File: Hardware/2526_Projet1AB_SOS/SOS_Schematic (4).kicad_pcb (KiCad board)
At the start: 2 copper layers, 64 x 64 mm, 42 parts, among them J1 USB_B_Mini, J2 Conn_02x10_Odd_Even, J3 Conn_01x02, SW1 SW_SPDT, U1 BU33SD5WG-TR, U2 STM32L476RGTx, U3 HTRC11001T, Y1 13,56MHz, Y2 8MHz

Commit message: Add files via upload
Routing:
- net +3.3V: track 236.7 -> 228.6 mm
- net GND: vias 13 -> 134
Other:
- board text added: "B"
- board text added: "Projet SOS"
- board text added: "T"

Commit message: Update KiCAD Schematic: SWD
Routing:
- added copper zone on In2.Cu, net GND
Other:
- copper layers 2 -> 4
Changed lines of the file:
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@@
 	(layers
 		(0 "F.Cu" signal)
+		(4 "In1.Cu" power "In1.Cu - VCC")
+		(6 "In2.Cu" power "In2.Cu -GND")
 		(2 "B.Cu" signal)
 		(9 "F.Adhes" user "F.Adhesive")
@@
 	)
 	(setup
+		(stackup
+			(layer "F.SilkS"
+				(type "Top Silk Screen")
+			)
+			(layer "F.Paste"
+				(type "Top Solder Paste")
+			)
+			(layer "F.Mask"
+				(type "Top Solder Mask")
+				(thickness 0.01)
+			)
+			(layer "F.Cu"
+				(type "copper")
+				(thickness 0.035)
+			)
+			(layer "dielectric 1"
+				(type "prepreg")
+				(thickness 0.1)
+				(material "FR4")
+				(epsilon_r 4.5)
+				(loss_tangent 0.02)
+			)
+			(layer "In1.Cu"
+				(type "copper")
+				(thickness 0.035)
+			)
+			(layer "dielectric 2"
+				(type "core")
+				(thickness 1.24)
+				(material "FR4")
+				(epsilon_r 4.5)
+				(loss_tangent 0.02)
+			)
+			(layer "In2.Cu"
+				(type "copper")
+				(thickness 0.035)
+			)
+			(layer "dielectric 3"
+				(type "prepreg")
+				(thickness 0.1)
+				(material "FR4")
+				(epsilon_r 4.5)
+				(loss_tangent 0.02)
+			)
+			(layer "B.Cu"
+				(type "copper")
+				(thickness 0.035)
+			)
+			(layer "B.Mask"
+				(type "Bottom Solder Mask")
+				(thickness 0.01)
+			)
+			(layer "B.Paste"
+				(type "Bottom Solder Paste")
+			)
+			(layer "B.SilkS"
+				(type "Bottom Silk Screen")
+			)
+			(copper_finish "None")
+			(dielectric_constraints no)
+		)
 		(pad_to_mask_clearance 0)
 		(allow_soldermask_bridges_in_footprints no)
@@
 			)
 		)
+	)
+	(zone
+		(net 1)
+		(net_name "GND")
+		(layer "In2.Cu")
+		(hatch edge 0.5)
+		(priority 1)
+		(connect_pads
+			(clearance 0.5)
+		)
+		(min_thickness 0.25)
+		(filled_areas_thickness no)
+		(fill yes
+			(thermal_gap 0.5)
+			(thermal_bridge_width 0.5)
+		)
+		(polygon
+			(pts
+				(xy 108 67) (xy 172 67) (xy 172 131) (xy 108 131)
+			)
+		)

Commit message: work on schematic and updating board
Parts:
- added R8: 5k1, Resistor_SMD:R_0805_2012Metric_Pad1.20x1.40mm_HandSolder, F.Cu at (157.0, 110.0)
- added R9: 5k1, Resistor_SMD:R_0805_2012Metric_Pad1.20x1.40mm_HandSolder, F.Cu at (157.0, 113.0)
- added U4: USBLC6-2SC6, Package_TO_SOT_SMD:SOT-23-6, F.Cu at (151.0, 111.0)
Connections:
- U2 pad 44: USBDM -> D-
- U2 pad 45: USBDP -> D+
- U2 pad 49: SWDCK -> SWCLK
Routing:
- net USBDM: track 52.4 -> 2.16 mm, vias 2 -> 1
- net D-: track 0.00 -> 49.7 mm, vias 0 -> 1
- net D+: track 0.00 -> 4.84 mm
- net GND: track 191.2 -> 186.6 mm, vias 134 -> 150
- net USBDP: track 44.3 -> 41.3 mm
- net SWDIO: track 30.1 -> 31.4 mm
- net Net-(J2-Pin_17): track 48.4 -> 47.8 mm

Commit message: schematic v2
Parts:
- removed C18, C20: 1u, Capacitor_SMD:C_0603_1608Metric_Pad1.08x0.95mm_HandSolder
- removed C19: 20p, Capacitor_SMD:C_0603_1608Metric_Pad1.08x0.95mm_HandSolder
- removed C8: 22p, Capacitor_SMD:C_0603_1608Metric_Pad1.08x0.95mm_HandSolder
- removed J1: USB_B_Mini, Connector_USB:USB_Mini-B_Tensility_54-00023_Vertical
- removed J3: Conn_01x02, Connector_JST:JST_XH_B2B-XH-A_1x02_P2.50mm_Vertical
- removed L1: 1/2 uH, Inductor_SMD:L_0805_2012Metric_Pad1.05x1.20mm_HandSolder
- removed L2: L_Small, Inductor_SMD:L_0805_2012Metric_Pad1.05x1.20mm_HandSolder
- removed U4: USBLC6-2SC6, Package_TO_SOT_SMD:SOT-23-6
- removed Y2: 8MHz, Crystal:Crystal_DS10_D1.0mm_L4.3mm_Vertical
- added D1: RED, LED_SMD:LED_0603_1608Metric, F.Cu at (91.6, 61.6)
- added D2: RED, LED_SMD:LED_0603_1608Metric, F.Cu at (91.6, 64.2)
- added D3: RED, LED_SMD:LED_0603_1608Metric, F.Cu at (96.2, 83.4)
- added D4: GREEN, LED_SMD:LED_0603_1608Metric, F.Cu at (96.2, 86.0)
- added D5: BLUE, LED_SMD:LED_0603_1608Metric, F.Cu at (96.0, 89.7)
- added R10: 10k, Resistor_SMD:R_0603_1608Metric, F.Cu at (67.0, 32.5)
- added R11: 1k6, Resistor_SMD:R_0603_1608Metric, F.Cu at (91.2, 82.5)
- added R12: 1k1, Resistor_SMD:R_0603_1608Metric, F.Cu at (91.2, 85.0)
- added R13: 10k, Resistor_SMD:R_0603_1608Metric, F.Cu at (67.0, 40.0)
- added R14: 670R, Resistor_SMD:R_0603_1608Metric, F.Cu at (91.2, 90.0)
- added R15: 10k, Resistor_SMD:R_0603_1608Metric, F.Cu at (67.0, 45.0)
- added RFID1: RC522, Connector_PinSocket_2.54mm:PinSocket_1x08_P2.54mm_Vertical, F.Cu at (66.1, 100.0)
- added SW2: SW_Push, Button_Switch_SMD:SW_SPST_B3S-1000, F.Cu at (61.4, 51.0)
- added SW3: SW_Push, Button_Switch_SMD:SW_SPST_B3S-1000, F.Cu at (69.8, 51.0)
- added SW4: SW_Push, Button_Switch_SMD:SW_SPST_B3S-1000, F.Cu at (78.2, 51.0)
- added SW5: SW_Push, Button_Switch_SMD:SW_SPST_B3S-1000, F.Cu at (86.7, 51.0)
- added TP4: TP_NSS, TestPoint:TestPoint_Pad_D1.0mm, F.Cu at (67.5, 93.3)
- added TP5: TP_SCK, TestPoint:TestPoint_Pad_D1.0mm, F.Cu at (69.9, 93.4)
- added TP6: TP_MOSI, TestPoint:TestPoint_Pad_D1.0mm, F.Cu at (72.0, 93.5)
- added TP7: TP_MISO, TestPoint:TestPoint_Pad_D1.0mm, F.Cu at (74.3, 93.6)
- added TP8: TP_IRQ, TestPoint:TestPoint_Pad_D1.0mm, F.Cu at (76.8, 93.5)
- added TP9: TP_RST, TestPoint:TestPoint_Pad_D1.0mm, F.Cu at (80.8, 94.7)
- added TP_3V3: TP_3V3, TestPoint:TestPoint_Pad_D1.0mm, F.Cu at (89.1, 70.8)
- added TP_5V1: TP_5V, TestPoint:TestPoint_Pad_D1.0mm, F.Cu at (89.1, 67.7)
- added TP_NRST1: TP_NRST, TestPoint:TestPoint_Pad_D1.0mm, F.Cu at (57.0, 66.0)
- C1, C11, C2: value 100n -> 1u; footprint Capacitor_SMD:C_0603_1608Metric_Pad1.08x0.95mm_HandSolder -> Capacitor_SMD:C_0603_1608Metric
- C10, C13, C15: footprint Capacitor_SMD:C_0603_1608Metric_Pad1.08x0.95mm_HandSolder -> Capacitor_SMD:C_0603_1608Metric
- C12: value 10n -> 100n; footprint Capacitor_SMD:C_0603_1608Metric_Pad1.08x0.95mm_HandSolder -> Capacitor_SMD:C_0603_1608Metric
- C14: value 100n -> 10n; footprint Capacitor_SMD:C_0603_1608Metric_Pad1.08x0.95mm_HandSolder -> Capacitor_SMD:C_0603_1608Metric
- C16: value 20p -> 10n; footprint Capacitor_SMD:C_0603_1608Metric_Pad1.08x0.95mm_HandSolder -> Capacitor_SMD:C_0603_1608Metric
- C17: value 1u -> 10n; footprint Capacitor_SMD:C_0603_1608Metric_Pad1.08x0.95mm_HandSolder -> Capacitor_SMD:C_0603_1608Metric
- C3: value 100n -> 4u7; footprint Capacitor_SMD:C_0603_1608Metric_Pad1.08x0.95mm_HandSolder -> Capacitor_SMD:C_0603_1608Metric
- C4: value 10u -> 20p; footprint Capacitor_SMD:C_0603_1608Metric_Pad1.08x0.95mm_HandSolder -> Capacitor_SMD:C_0603_1608Metric
- C5: value 1,5n -> 100n; footprint Capacitor_SMD:C_0603_1608Metric_Pad1.08x0.95mm_HandSolder -> Capacitor_SMD:C_0603_1608Metric
- C6: value 22p -> 100n; footprint Capacitor_SMD:C_0603_1608Metric_Pad1.08x0.95mm_HandSolder -> Capacitor_SMD:C_0603_1608Metric
- C7: value 100n -> 20p; footprint Capacitor_SMD:C_0603_1608Metric_Pad1.08x0.95mm_HandSolder -> Capacitor_SMD:C_0603_1608Metric
- C9: value 4,7u -> 100n; footprint Capacitor_SMD:C_0603_1608Metric_Pad1.08x0.95mm_HandSolder -> Capacitor_SMD:C_0603_1608Metric
- H1, H2, H3, H4: footprint MountingHole:MountingHole_3.2mm_M3_DIN965_Pad -> MountingHole:MountingHole_3.2mm_M3_Pad
- J2: value Conn_02x10_Odd_Even -> Conn_ST_STDC14; footprint Connector_PinHeader_1.27mm:PinHeader_2x10_P1.27mm_Vertical_SMD -> Connector_PinHeader_1.27mm:PinHeader_2x07_P1.27mm_Vertical_SMD
- R1: value 2,2k -> 5k1; footprint Resistor_SMD:R_0805_2012Metric_Pad1.20x1.40mm_HandSolder -> Resistor_SMD:R_0603_1608Metric
- R2: value 10k -> 5k1; footprint Resistor_SMD:R_0805_2012Metric_Pad1.20x1.40mm_HandSolder -> Resistor_SMD:R_0603_1608Metric
- R3: value 100K -> 3k3; footprint Resistor_SMD:R_0805_2012Metric_Pad1.20x1.40mm_HandSolder -> Resistor_SMD:R_0603_1608Metric
- R4: value 10k -> 1k6; footprint Resistor_SMD:R_0805_2012Metric_Pad1.20x1.40mm_HandSolder -> Resistor_SMD:R_0603_1608Metric
- R5: value 10k -> 390; footprint Resistor_SMD:R_0805_2012Metric_Pad1.20x1.40mm_HandSolder -> Resistor_SMD:R_0603_1608Metric
- R6: footprint Resistor_SMD:R_0805_2012Metric_Pad1.20x1.40mm_HandSolder -> Resistor_SMD:R_0603_1608Metric
- R7: value 390 -> 10k; footprint Resistor_SMD:R_0805_2012Metric_Pad1.20x1.40mm_HandSolder -> Resistor_SMD:R_0603_1608Metric
- R8, R9: value 5k1 -> 10k; footprint Resistor_SMD:R_0805_2012Metric_Pad1.20x1.40mm_HandSolder -> Resistor_SMD:R_0603_1608Metric
- U2: value STM32L476RGTx -> USBLC6-2SC6; footprint Package_QFP:LQFP-64_10x10mm_P0.5mm -> Package_TO_SOT_SMD:SOT-23-6
- U3: value HTRC11001T -> STM32L476RGTx; footprint Package_SO:SOIC-14_3.9x8.7mm_P1.27mm -> Package_QFP:LQFP-64_10x10mm_P0.5mm
- Y1: value 13,56MHz -> 20MHz; footprint Crystal:Crystal_DS10_D1.0mm_L4.3mm_Vertical -> Crystal:Crystal_SMD_HC49-SD
- moved R9 122.4 mm to (67.0, 29.9)
- moved J2 119.6 mm to (51.0, 63.2)
- moved H2 118.0 mm to (50.0, 100.0)
- moved C7 109.2 mm to (55.8, 79.5)
- moved R6 108.3 mm to (65.8, 81.0)
- moved R8 108.2 mm to (74.0, 40.5)
- moved C16 98.3 mm to (70.0, 35.5)
- moved R7 96.9 mm to (74.0, 38.0)
- moved U1 93.1 mm to (84.2, 66.7)
- moved R4 88.1 mm to (84.2, 63.0)
- moved C17 86.8 mm to (70.0, 38.0)
- moved C4 86.7 mm to (55.8, 72.0)
- moved C5 86.6 mm to (65.8, 74.0)
- moved C12 79.9 mm to (70.8, 66.5)
- moved R5 78.9 mm to (55.8, 76.0)
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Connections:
- C1 pad 1: GND -> +5V
- C1 pad 2: +3.3V -> GND
- C12 pad 2: +3.3VA -> +3.3V
- C13 pad 1: +3.3VA -> +3.3V
- C14 pad 1: +3.3V -> /USR_BTN_1
- C15 pad 1: GND -> NRST
- C15 pad 2: +3.3V -> GND
- C16 pad 1: GND -> /USR_BTN_2
- C16 pad 2: OSC_IN -> GND
- C17 pad 1: +5V -> /USR_BTN_3
- C2 pad 1: Net-(U3-QGND) -> +3.3V
- C3 pad 1: Net-(U3-CEXT) -> GND
- C3 pad 2: GND -> +3.3V
- C4 pad 2: +3.3V -> OSC_IN
- C5 pad 1: Net-(U3-TX2) -> +3.3V
- C5 pad 2: Net-(C5-Pad2) -> GND
- C6 pad 1: Net-(U3-XTAL2) -> +3.3V
- C7 pad 1: GND -> Net-(C7-Pad1)
- C7 pad 2: NRST -> GND
- C9 pad 1: GND -> +3.3V
- C9 pad 2: +3.3V -> GND
- J2 pad 1: +3.3V -> unconnected-(J2-NC-Pad1)
- J2 pad 10: GND -> unconnected-(J2-JTDI/NC-Pad10)
- J2 pad 11: Net-(J2-Pin_11) -> GND
- J2 pad 12: GND -> NRST
- J2 pad 13: TDO -> UART_RX
- J2 pad 14: GND -> UART_TX
- J2 pad 2: +3.3V -> unconnected-(J2-NC-Pad2)
- J2 pad 3: TRST -> +3.3V
- J2 pad 4: GND -> SWDIO
- J2 pad 5: TDI -> GND
- J2 pad 6: GND -> SWCLK
- J2 pad 7: SWDIO -> GND
- J2 pad 8: GND -> SWO
- J2 pad 9: SWDCK -> unconnected-(J2-JRCLK/NC-Pad9)
- R1 pad 1: Net-(C5-Pad2) -> Net-(J1-CC1)
- R1 pad 2: Net-(U3-RX) -> GND
- R2 pad 2: Net-(U2-BOOT0) -> Net-(J1-CC2)
- R3 pad 1: Net-(J1-ID) -> +5V
- R3 pad 2: GND -> Net-(D1-A)
- R4 pad 1: GND -> +3.3V
- R4 pad 2: Net-(J2-Pin_11) -> Net-(D2-A)
- R5 pad 1: GND -> OSC_OUT
- R5 pad 2: Net-(J2-Pin_17) -> Net-(C7-Pad1)
- R6 pad 1: Net-(J2-Pin_19) -> GND
- R6 pad 2: GND -> Net-(U3-BOOT0)
- R7 pad 1: OSC_OUT -> /USR_BTN_1
- R7 pad 2: Net-(C19-Pad1) -> Net-(R7-Pad2)
- R8 pad 1: Net-(J5-CC1) -> Net-(R7-Pad2)
- R9 pad 1: GND -> /USR_BTN_2
- U2 pad 1: +3.3V -> USBDP
- U2 pad 2: unconnected-(U2-PC13-Pad2) -> GND
- U2 pad 3: unconnected-(U2-PC14-Pad3) -> USBDM
- U2 pad 4: unconnected-(U2-PC15-Pad4) -> D+
- U2 pad 5: OSC_IN -> +5V
- U2 pad 6: OSC_OUT -> D-
- U3 pad 1: GND -> +3.3V
- U3 pad 10: SPI1_MISO -> unconnected-(U3-PC2-Pad10)
- U3 pad 11: (no net) -> unconnected-(U3-PC3-Pad11)
- U3 pad 12: Net-(U3-CEXT) -> GND
- U3 pad 13: Net-(U3-QGND) -> +3.3V
- U3 pad 14: Net-(U3-RX) -> unconnected-(U3-PA0-Pad14)
- U3 pad 2: Net-(U3-TX2) -> unconnected-(U3-PC13-Pad2)
- U3 pad 3: +3.3V -> unconnected-(U3-PC14-Pad3)
- U3 pad 4: Net-(U3-TX1) -> unconnected-(U3-PC15-Pad4)
- U3 pad 5: GND -> OSC_IN
- U3 pad 6: Net-(U3-XTAL1) -> OSC_OUT
- U3 pad 7: Net-(U3-XTAL2) -> NRST
- U3 pad 8: SPI1_SCK -> unconnected-(U3-PC0-Pad8)
- U3 pad 9: SPI1_MOSI -> unconnected-(U3-PC1-Pad9)
- Y1 pad 1: Net-(U3-XTAL2) -> Net-(C7-Pad1)
- Y1 pad 2: Net-(U3-XTAL1) -> OSC_IN
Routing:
- net +3.3V: track 229.0 -> 0.00 mm, vias 2 -> 0
- net GND: track 186.6 -> 0.00 mm, vias 150 -> 0
- net +5V: track 107.4 -> 0.00 mm, vias 2 -> 0
- net Net-(C5-Pad2): track 65.1 -> 0.00 mm, vias 2 -> 0
- net SPI1_SCK: track 63.6 -> 0.00 mm
- net +3.3VA: track 58.9 -> 0.00 mm, vias 2 -> 0
- net Net-(U3-XTAL1): track 57.6 -> 0.00 mm, vias 2 -> 0
- net D-: track 49.7 -> 0.00 mm, vias 1 -> 0
- net Net-(J2-Pin_17): track 47.8 -> 0.00 mm, vias 2 -> 0
- net USBDP: track 41.3 -> 0.00 mm, vias 2 -> 0
- net Net-(U3-XTAL2): track 41.2 -> 0.00 mm, vias 1 -> 0
- net NRST: track 37.7 -> 0.00 mm, vias 2 -> 0
- net Net-(U3-TX1): track 32.9 -> 0.00 mm
- net SWDIO: track 31.4 -> 0.00 mm, vias 2 -> 0
- net Net-(SW1-B): track 31.2 -> 0.00 mm
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- added copper zone on In1.Cu, net +3.3V
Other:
- board size 64 x 64 mm -> 58 x 58 mm
- board text removed: "B"
- board text removed: "Projet SOS"
- board text removed: "T"

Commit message: BOM
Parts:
- TP_3V3: value TP_3V3 -> TestPoint
- TP_5V1: value TP_5V -> TestPoint
- TP_IRQ1: renamed from TP8; value TP_IRQ -> TestPoint
- TP_MISO1: renamed from TP7; value TP_MISO -> TestPoint
- TP_MOSI1: renamed from TP6; value TP_MOSI -> TestPoint
- TP_NRST1: value TP_NRST -> TestPoint
- TP_NSS1: renamed from TP4; value TP_NSS -> TestPoint
- TP_RST1: renamed from TP9; value TP_RST -> TestPoint
- TP_SCK1: renamed from TP5; value TP_SCK -> TestPoint
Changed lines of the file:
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@@
 		(descr "SMD pad as test Point, diameter 1.0mm")
 		(tags "test point SMD pad")
-		(property "Reference" "TP5"
+		(property "Reference" "TP_SCK1"
 			(at 0 -1.448 0)
 			(layer "F.SilkS")
@@
 			)
 		)
-		(property "Value" "TP_SCK"
+		(property "Value" "TestPoint"
 			(at 0 1.55 0)
 			(layer "F.Fab")
@@
 			)
 		)
-		(property "Value" "TP_5V"
+		(property "Value" "TestPoint"
 			(at 0 1.55 0)
 			(layer "F.Fab")
@@
 		(descr "SMD pad as test Point, diameter 1.0mm")
 		(tags "test point SMD pad")
-		(property "Reference" "TP9"
+		(property "Reference" "TP_RST1"
 			(at 0 -1.448 0)
 			(layer "F.SilkS")
@@
 			)
 		)
-		(property "Value" "TP_RST"
+		(property "Value" "TestPoint"
 			(at 0 1.55 0)
 			(layer "F.Fab")
@@
 		(descr "SMD pad as test Point, diameter 1.0mm")
 		(tags "test point SMD pad")
-		(property "Reference" "TP4"
+		(property "Reference" "TP_NSS1"
 			(at 0 -1.448 0)
 			(layer "F.SilkS")
@@
 			)
 		)
-		(property "Value" "TP_NSS"
+		(property "Value" "TestPoint"
 			(at 0 1.55 0)
 			(layer "F.Fab")
@@
 		(descr "SMD pad as test Point, diameter 1.0mm")
 		(tags "test point SMD pad")
-		(property "Reference" "TP7"
+		(property "Reference" "TP_MISO1"
 			(at 0 -1.448 0)
 			(layer "F.SilkS")
@@
 			)
 		)
-		(property "Value" "TP_MISO"
+		(property "Value" "TestPoint"
 			(at 0 1.55 0)
 			(layer "F.Fab")
@@
 			)
 		)
-		(property "Value" "TP_NRST"
+		(property "Value" "TestPoint"
 			(at 0 1.55 0)
 			(layer "F.Fab")
@@
 			)
 		)
-		(property "Value" "TP_3V3"
+		(property "Value" "TestPoint"
 			(at 0 1.55 0)
 			(layer "F.Fab")
@@
 		(descr "SMD pad as test Point, diameter 1.0mm")
 		(tags "test point SMD pad")
-		(property "Reference" "TP6"
+		(property "Reference" "TP_MOSI1"
 			(at 0 -1.448 0)
 			(layer "F.SilkS")
@@
 			)
 		)
-		(property "Value" "TP_MOSI"
+		(property "Value" "TestPoint"
 			(at 0 1.55 0)
 			(layer "F.Fab")
@@
 		(descr "SMD pad as test Point, diameter 1.0mm")
 		(tags "test point SMD pad")
-		(property "Reference" "TP8"
+		(property "Reference" "TP_IRQ1"
 			(at 0 -1.448 0)
 			(layer "F.SilkS")
@@
 			)
 		)
-		(property "Value" "TP_IRQ"
+		(property "Value" "TestPoint"
 			(at 0 1.55 0)
 			(layer "F.Fab")

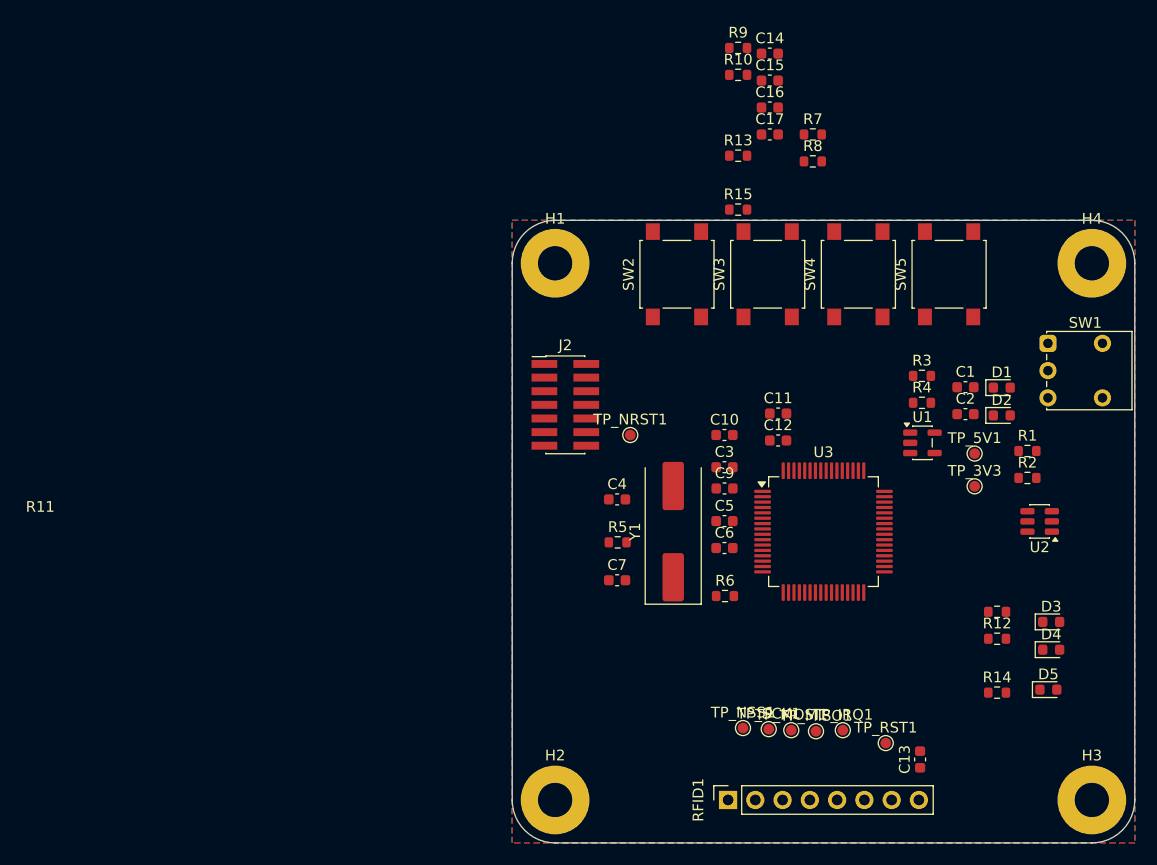
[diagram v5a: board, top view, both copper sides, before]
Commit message: Routage Board (sauf port USB)
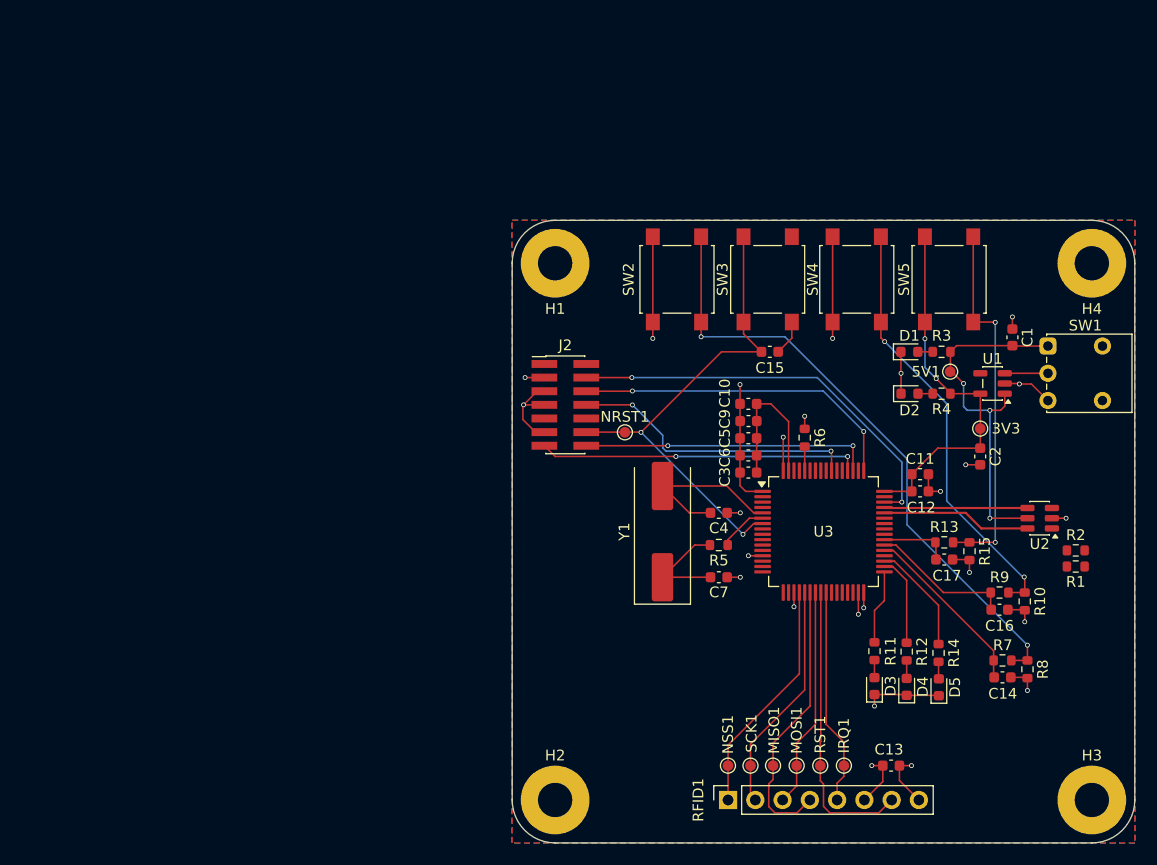
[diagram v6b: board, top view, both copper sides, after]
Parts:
- moved C14 62.0 mm to (91.7, 88.6)
- moved R9 56.3 mm to (91.4, 80.7)
- moved R10 55.8 mm to (93.8, 81.5), turned to -90 degrees
- moved R7 52.1 mm to (91.7, 87.0)
- moved C16 51.4 mm to (91.4, 82.3)
- moved R8 51.4 mm to (94.0, 87.8), turned to -90 degrees
- moved C17 42.8 mm to (86.2, 77.6)
- moved R13 40.8 mm to (86.2, 76.0)
- moved R15 38.4 mm to (88.6, 76.8), turned to -90 degrees
- moved C15 25.3 mm to (70.0, 58.2)
- moved D3 17.5 mm to (79.8, 89.4), turned to 90 degrees
- moved R6 16.5 mm to (73.2, 66.2), turned to -90 degrees
- moved C11 14.4 mm to (84.0, 69.7)
- moved C12 14.0 mm to (84.0, 71.2), turned to 180 degrees
- moved D4 13.9 mm to (82.8, 89.5), turned to 90 degrees
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- renumbered TP_3V3 to 3V3, TP_5V1 to 5V1, TP_IRQ1 to IRQ1, TP_MISO1 to MISO1, TP_MOSI1 to MOSI1, TP_NRST1 to NRST1, TP_NSS1 to NSS1, TP_RST1 to RST1, TP_SCK1 to SCK1
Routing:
- net +3.3V: track 0.00 -> 79.6 mm, vias 0 -> 11
- net GND: track 0.00 -> 67.1 mm, vias 0 -> 16
- net Net-(R7-Pad2): track 0.00 -> 58.1 mm, vias 0 -> 2
- net NRST: track 0.00 -> 46.5 mm, vias 0 -> 2
- net Net-(R10-Pad1): track 0.00 -> 40.3 mm, vias 0 -> 2
- net SWDIO: track 0.00 -> 38.0 mm, vias 0 -> 2
- net Net-(R13-Pad2): track 0.00 -> 34.4 mm, vias 0 -> 2
- net +5V: track 0.00 -> 33.8 mm, vias 0 -> 3
- net SWCLK: track 0.00 -> 31.1 mm, vias 0 -> 2
- net UART_RX: track 0.00 -> 30.0 mm, vias 0 -> 2
- net UART_TX: track 0.00 -> 27.2 mm, vias 0 -> 2
- net RC522_RST: track 0.00 -> 27.2 mm
- net SWO: track 0.00 -> 27.1 mm, vias 0 -> 2
- net SPI1_MISO: track 0.00 -> 26.1 mm
- net SPI1_CS: track 0.00 -> 22.1 mm
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
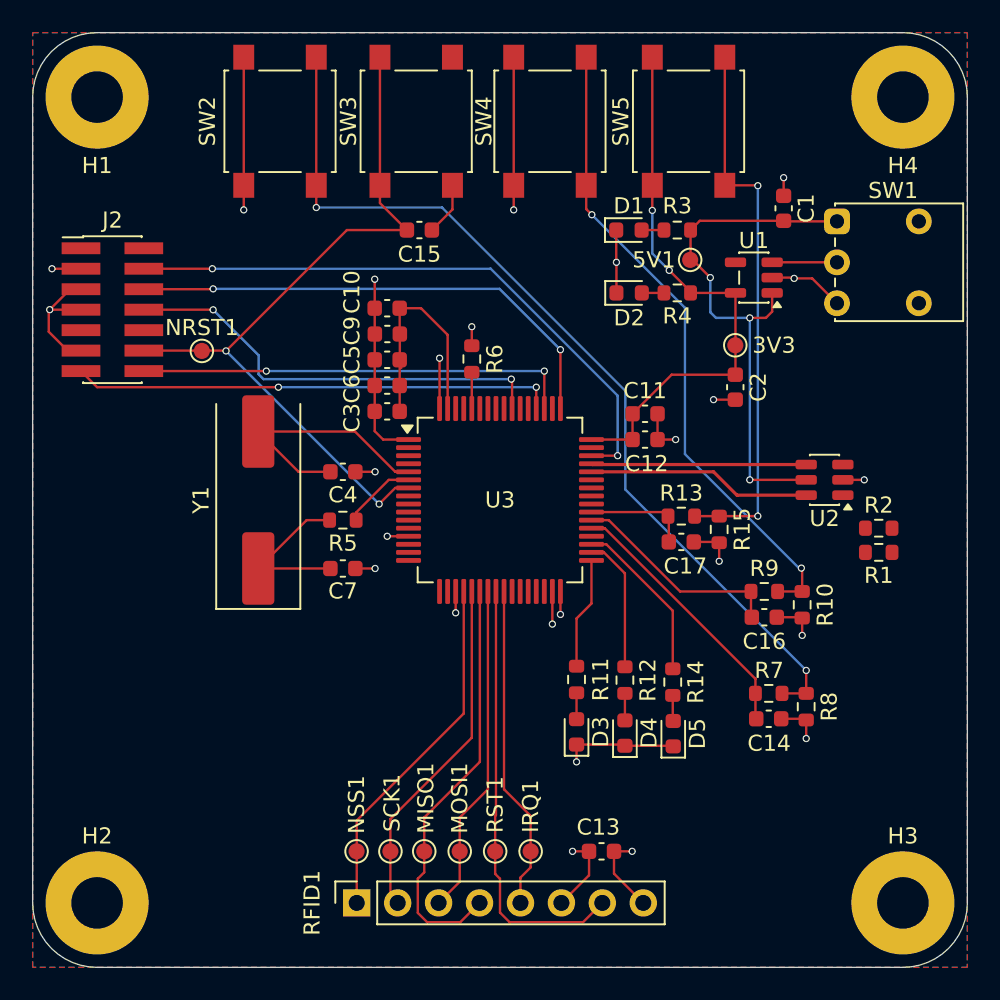
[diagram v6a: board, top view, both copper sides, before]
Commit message: USB and board routing
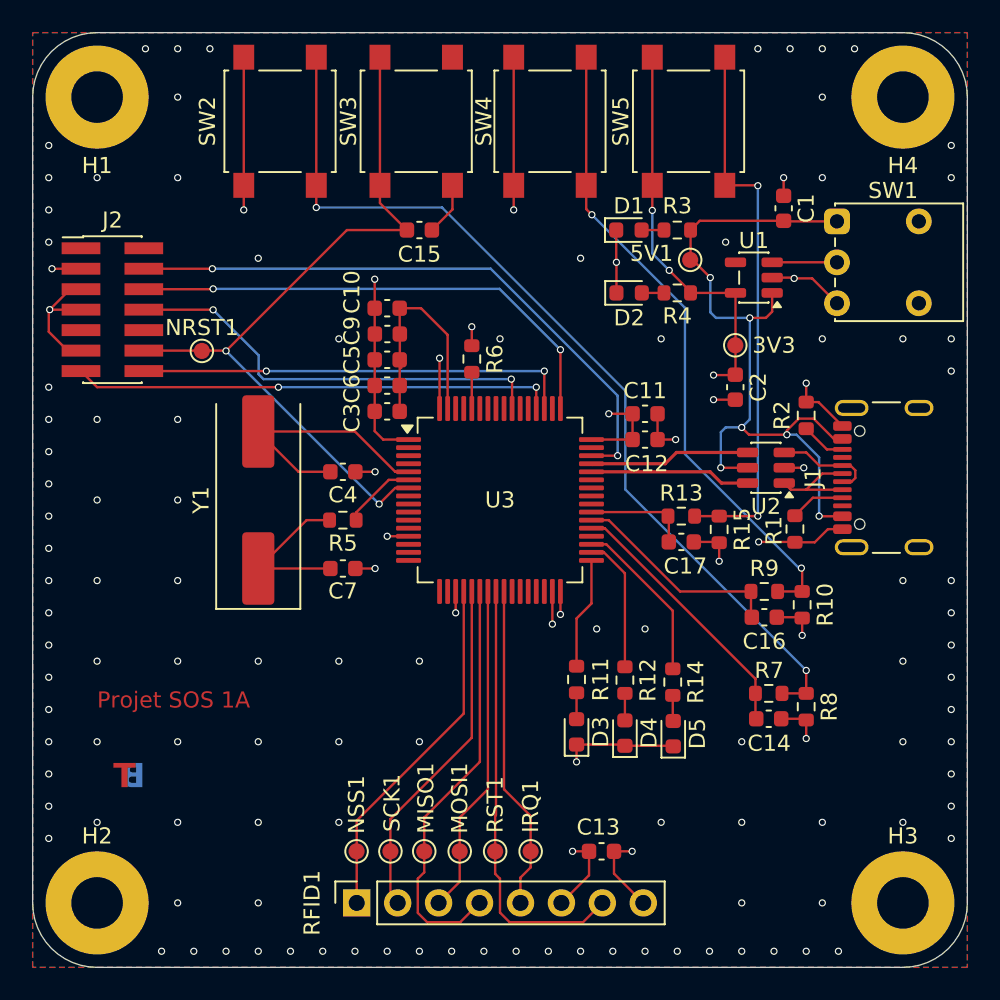
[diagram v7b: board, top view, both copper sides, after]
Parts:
- added J1: USB_C_Receptacle_USB2.0_16P, Connector_USB:USB_C_Receptacle_GCT_USB4105-xx-A_16P_TopMnt_Horizontal, F.Cu at (99.9, 73.6)
- moved R2 8.32 mm to (94.0, 69.8), turned to -90 degrees
- moved R1 5.40 mm to (93.3, 76.8), turned to -90 degrees
- moved U2 3.71 mm to (91.5, 73.0)
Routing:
- net +5V: track 33.8 -> 47.7 mm, vias 3 -> 6
- net GND: track 67.1 -> 76.6 mm, vias 16 -> 126
- net USBDP: track 0.00 -> 6.44 mm
- net USBDM: track 0.00 -> 6.24 mm
- net +3.3V: track 79.6 -> 75.1 mm, vias 11 -> 13
- net D-: track 13.9 -> 9.98 mm
- net Net-(J1-CC1): track 0.00 -> 3.41 mm
- net D+: track 13.3 -> 10.0 mm
- net Net-(J1-CC2): track 0.00 -> 2.78 mm
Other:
- board text added: "B"
- board text added: "GND"
- board text added: "Projet SOS 1A"
- board text added: "T"
- board text added: "VCC"
